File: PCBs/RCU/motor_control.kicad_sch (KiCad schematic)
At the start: 36 parts

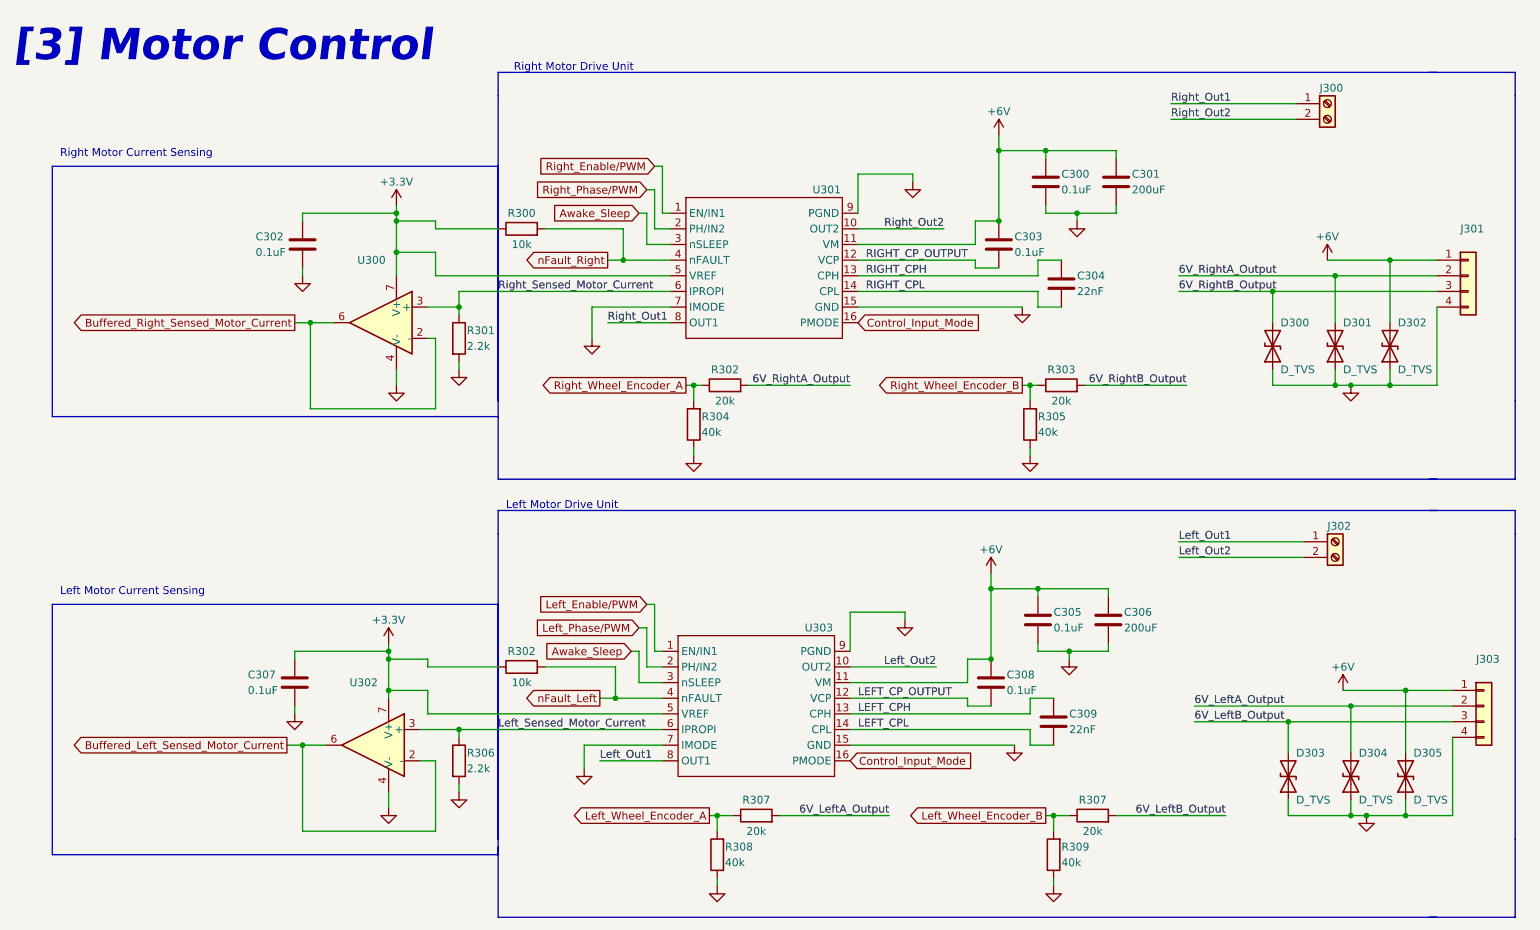
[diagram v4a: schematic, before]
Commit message: Add footprint to rest of IC's except ESP32
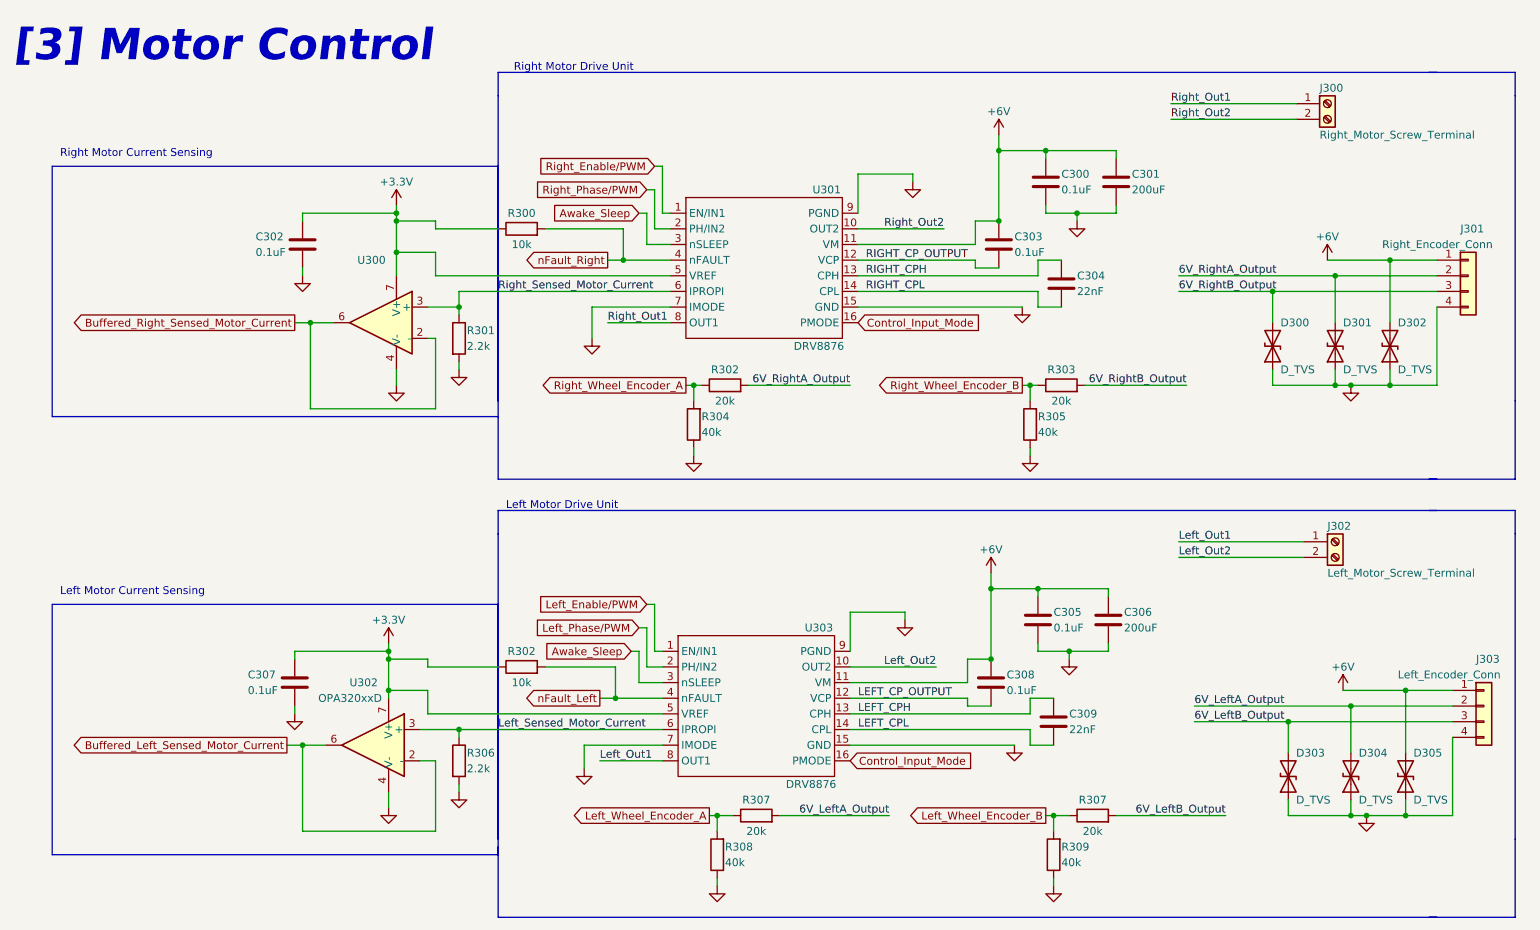
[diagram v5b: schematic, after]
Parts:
- J300: value (none) -> Right_Motor_Screw_Terminal; footprint (none) -> TerminalBlock:TerminalBlock_bornier-2_P5.08mm
- J301: value (none) -> Right_Encoder_Conn; footprint (none) -> Connector_PinHeader_2.54mm:PinHeader_1x04_P2.54mm_Vertical
- J302: value (none) -> Left_Motor_Screw_Terminal; footprint (none) -> TerminalBlock:TerminalBlock_bornier-2_P5.08mm
- J303: value (none) -> Left_Encoder_Conn; footprint (none) -> Connector_PinHeader_2.54mm:PinHeader_1x04_P2.54mm_Vertical
- U301, U303: value (none) -> DRV8876; footprint (none) -> Package_SO:HTSSOP-16-1EP_4.4x5mm_P0.65mm_EP3.4x5mm_Mask2.46x2.31mm_ThermalVias
- U302: value (none) -> OPA320xxD; footprint (none) -> Package_TO_SOT_SMD:SOT-23-5
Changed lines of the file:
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@@
     (in_bom yes) (on_board yes)
     (property "Reference" "U301" (id 0) (at 156.21 44.45 0))
-    (property "Value" "" (id 1) (at 154.94 69.85 0))
-    (property "Footprint" "" (id 2) (at 146.05 55.88 0)
+    (property "Value" "DRV8876" (id 1) (at 154.94 69.85 0))
+    (property "Footprint" "Package_SO:HTSSOP-16-1EP_4.4x5mm_P0.65mm_EP3.4x5mm_Mask2.46x2.31mm_ThermalVias" (id 2) (at 146.05 55.88 0)
       (effects (font (size 1.27 1.27)) hide)
     )
@@
       (effects (font (size 1.27 1.27)) (justify left))
     )
-    (property "Value" "" (id 1) (at 237.49 106.68 0)
-      (effects (font (size 1.27 1.27)) (justify left))
-    )
-    (property "Footprint" "" (id 2) (at 238.76 101.6 0)
+    (property "Value" "Left_Motor_Screw_Terminal" (id 1) (at 237.49 106.68 0)
+      (effects (font (size 1.27 1.27)) (justify left))
+    )
+    (property "Footprint" "TerminalBlock:TerminalBlock_bornier-2_P5.08mm" (id 2) (at 238.76 101.6 0)
       (effects (font (size 1.27 1.27)) hide)
     )
@@
       (effects (font (size 1.27 1.27)) (justify left))
     )
-    (property "Value" "" (id 1) (at 236.22 35.56 0)
-      (effects (font (size 1.27 1.27)) (justify left))
-    )
-    (property "Footprint" "" (id 2) (at 237.49 30.48 0)
+    (property "Value" "Right_Motor_Screw_Terminal" (id 1) (at 236.22 35.56 0)
+      (effects (font (size 1.27 1.27)) (justify left))
+    )
+    (property "Footprint" "TerminalBlock:TerminalBlock_bornier-2_P5.08mm" (id 2) (at 237.49 30.48 0)
       (effects (font (size 1.27 1.27)) hide)
     )
@@
       (effects (font (size 1.27 1.27)) (justify left))
     )
-    (property "Value" "" (id 1) (at 248.92 123.19 0)
-      (effects (font (size 1.27 1.27)) (justify left))
-    )
-    (property "Footprint" "" (id 2) (at 262.89 128.27 0)
+    (property "Value" "Left_Encoder_Conn" (id 1) (at 248.92 123.19 0)
+      (effects (font (size 1.27 1.27)) (justify left))
+    )
+    (property "Footprint" "Connector_PinHeader_2.54mm:PinHeader_1x04_P2.54mm_Vertical" (id 2) (at 262.89 128.27 0)
       (effects (font (size 1.27 1.27)) hide)
     )
@@
       (effects (font (size 1.27 1.27)) (justify left))
     )
-    (property "Value" "" (id 1) (at 246.38 53.34 0)
-      (effects (font (size 1.27 1.27)) (justify left))
-    )
-    (property "Footprint" "" (id 2) (at 260.35 58.42 0)
+    (property "Value" "Right_Encoder_Conn" (id 1) (at 246.38 53.34 0)
+      (effects (font (size 1.27 1.27)) (justify left))
+    )
+    (property "Footprint" "Connector_PinHeader_2.54mm:PinHeader_1x04_P2.54mm_Vertical" (id 2) (at 260.35 58.42 0)
       (effects (font (size 1.27 1.27)) hide)
     )
@@
     (in_bom yes) (on_board yes)
     (property "Reference" "U303" (id 0) (at 154.94 115.57 0))
-    (property "Value" "" (id 1) (at 153.67 140.97 0))
-    (property "Footprint" "" (id 2) (at 144.78 127 0)
+    (property "Value" "DRV8876" (id 1) (at 153.67 140.97 0))
+    (property "Footprint" "Package_SO:HTSSOP-16-1EP_4.4x5mm_P0.65mm_EP3.4x5mm_Mask2.46x2.31mm_ThermalVias" (id 2) (at 144.78 127 0)
       (effects (font (size 1.27 1.27)) hide)
     )
@@
       (effects (font (size 1.27 1.27)) (justify right))
     )
-    (property "Value" "" (id 1) (at 73.66 127 0)
-      (effects (font (size 1.27 1.27)) (justify right))
-    )
-    (property "Footprint" "" (id 2) (at 85.09 139.7 0)
+    (property "Value" "OPA320xxD" (id 1) (at 73.66 127 0)
+      (effects (font (size 1.27 1.27)) (justify right))
+    )
+    (property "Footprint" "Package_TO_SOT_SMD:SOT-23-5" (id 2) (at 85.09 139.7 0)
       (effects (font (size 1.27 1.27)) (justify left) hide)
     )

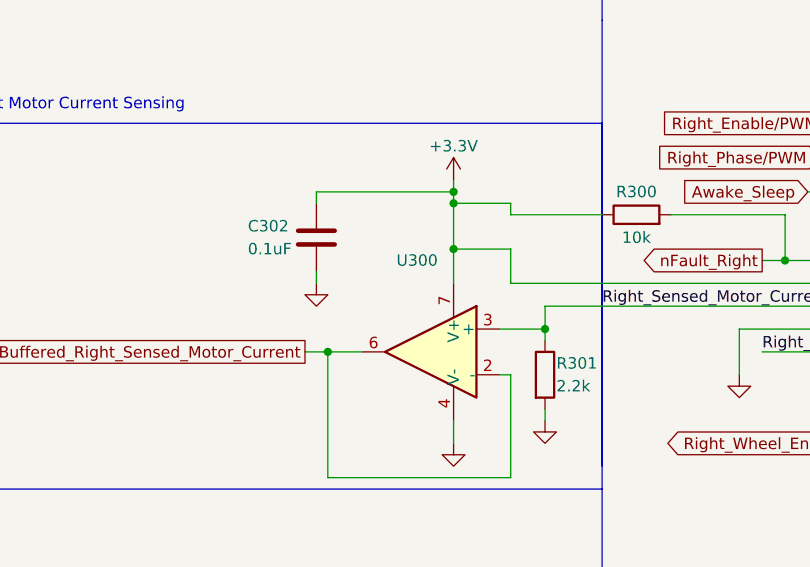
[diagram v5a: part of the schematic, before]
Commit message: Add footprint to power module diodes, and replaced 1N4148W with 2 SM5817's
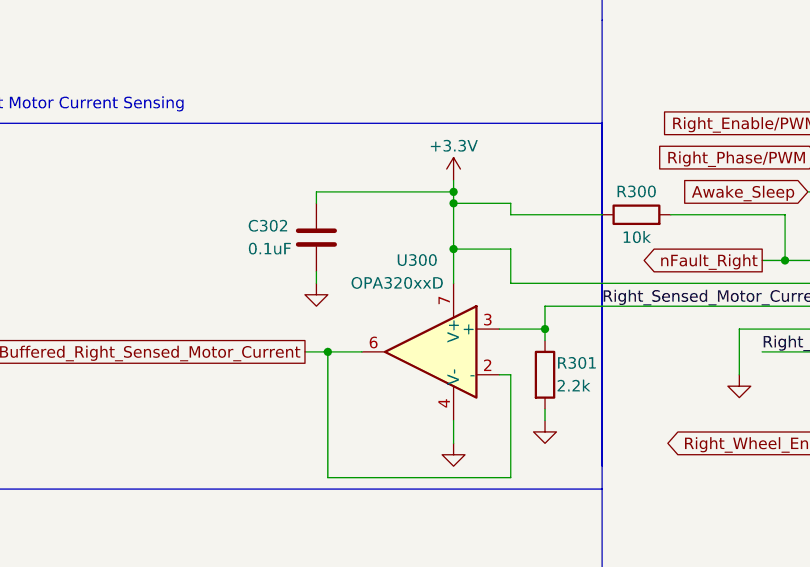
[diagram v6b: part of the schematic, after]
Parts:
- U300: value (none) -> OPA320xxD; footprint (none) -> Package_TO_SOT_SMD:SOT-23-5
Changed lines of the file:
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@@
       (effects (font (size 1.27 1.27)) (justify right))
     )
-    (property "Value" "" (id 1) (at 74.93 58.42 0)
+    (property "Value" "OPA320xxD" (id 1) (at 74.93 58.42 0)
       (effects (font (size 1.27 1.27)) (justify right))
     )
-    (property "Footprint" "" (id 2) (at 86.36 71.12 0)
+    (property "Footprint" "Package_TO_SOT_SMD:SOT-23-5" (id 2) (at 86.36 71.12 0)
       (effects (font (size 1.27 1.27)) (justify left) hide)
     )

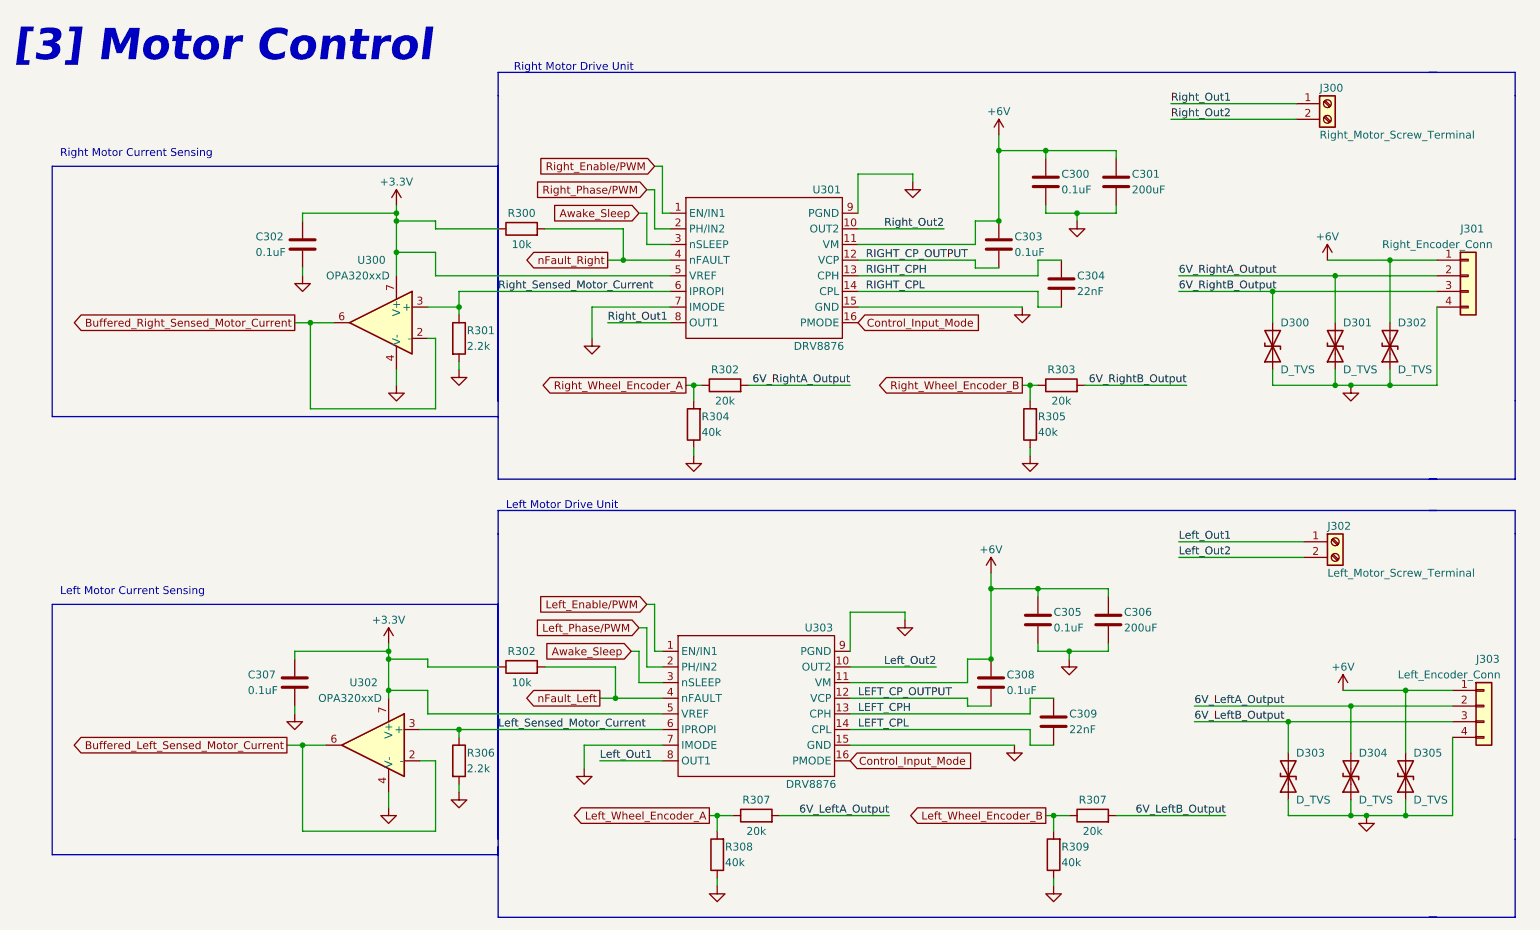
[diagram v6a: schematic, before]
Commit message: Add footrpints to TVS diodes in [3]
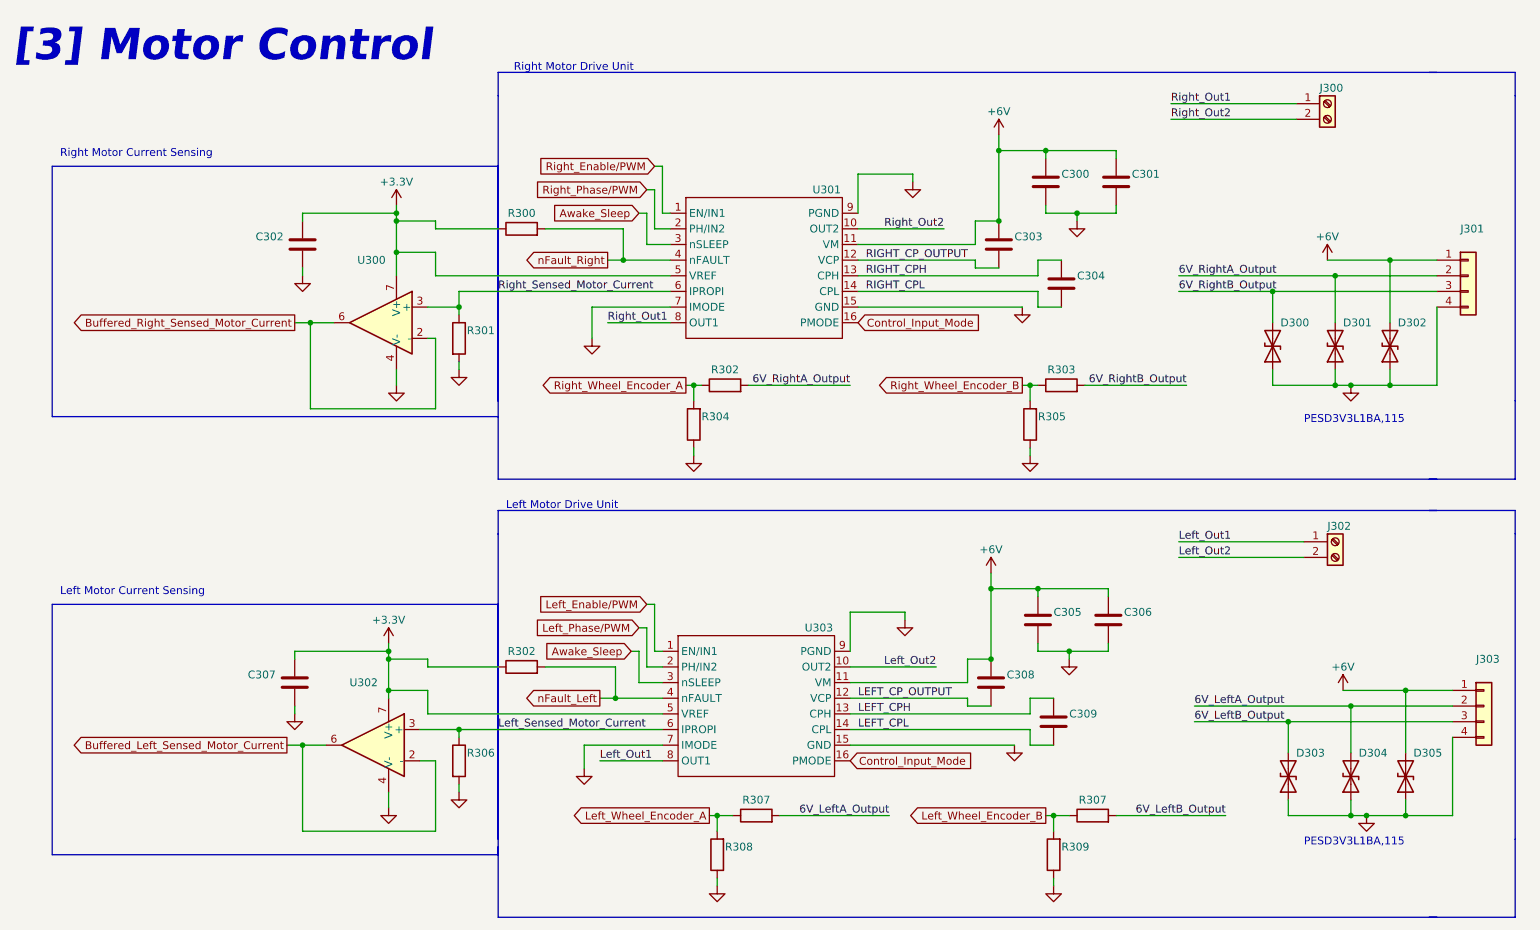
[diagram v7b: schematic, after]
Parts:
- C300, C302, C303, C305, C307, C308: value 0.1uF -> (none)
- C301, C306: value 200uF -> (none)
- C304, C309: value 22nF -> (none)
- D300, D301, D302, D303, D304, D305: value D_TVS -> (none)
- J300: value Right_Motor_Screw_Terminal -> (none); footprint TerminalBlock:TerminalBlock_bornier-2_P5.08mm -> (none)
- J301: value Right_Encoder_Conn -> (none); footprint Connector_PinHeader_2.54mm:PinHeader_1x04_P2.54mm_Vertical -> (none)
- J302: value Left_Motor_Screw_Terminal -> (none); footprint TerminalBlock:TerminalBlock_bornier-2_P5.08mm -> (none)
- J303: value Left_Encoder_Conn -> (none); footprint Connector_PinHeader_2.54mm:PinHeader_1x04_P2.54mm_Vertical -> (none)
- R300, R302: value 10k -> (none)
- R301, R306: value 2.2k -> (none)
- R302, R303, R307: value 20k -> (none)
- R304, R305, R308, R309: value 40k -> (none)
- U300, U302: value OPA320xxD -> (none); footprint Package_TO_SOT_SMD:SOT-23-5 -> (none)
- U301, U303: value DRV8876 -> (none); footprint Package_SO:HTSSOP-16-1EP_4.4x5mm_P0.65mm_EP3.4x5mm_Mask2.46x2.31mm_ThermalVias -> (none)
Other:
- note added: "PESD3V3L1BA,115"

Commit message: Passed ERC
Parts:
- C300, C302, C303, C305, C307, C308: value (none) -> 0.1uF; footprint (none) -> Capacitor_SMD:C_0603_1608Metric
- C301, C306: value (none) -> 220uF; footprint (none) -> Capacitor_THT:CP_Radial_D5.0mm_P2.50mm
- C304, C309: value (none) -> 22nF; footprint (none) -> Capacitor_SMD:C_0603_1608Metric
- D300, D301, D302, D303, D304, D305: value (none) -> PESD3V3L1BA,115; footprint (none) -> Diode_SMD:D_SOD-323
- J300: value (none) -> Right_Motor_Screw_Terminal; footprint (none) -> TerminalBlock:TerminalBlock_bornier-2_P5.08mm
- J301: value (none) -> Right_Encoder_Conn; footprint (none) -> Connector_PinHeader_2.54mm:PinHeader_1x04_P2.54mm_Vertical
- J302: value (none) -> Left_Motor_Screw_Terminal; footprint (none) -> TerminalBlock:TerminalBlock_bornier-2_P5.08mm
- J303: value (none) -> Left_Encoder_Conn; footprint (none) -> Connector_PinHeader_2.54mm:PinHeader_1x04_P2.54mm_Vertical
- R300: value (none) -> 10k; footprint (none) -> Resistor_SMD:R_0603_1608Metric
- R301: value (none) -> 2.2k; footprint (none) -> Resistor_SMD:R_0603_1608Metric
- R302, R303: value (none) -> 20k; footprint (none) -> Resistor_SMD:R_0603_1608Metric
- R304, R305: value (none) -> 40k; footprint (none) -> Resistor_SMD:R_0603_1608Metric
- R306: renamed from R302; value (none) -> 10k; footprint (none) -> Resistor_SMD:R_0603_1608Metric
- R307: renamed from R306; value (none) -> 2.2k; footprint (none) -> Resistor_SMD:R_0603_1608Metric
- R309: renamed from R307; value (none) -> 20k; footprint (none) -> Resistor_SMD:R_0603_1608Metric
- R310: renamed from R308; value (none) -> 40k; footprint (none) -> Resistor_SMD:R_0603_1608Metric
- R311: renamed from R309; value (none) -> 40k; footprint (none) -> Resistor_SMD:R_0603_1608Metric
- U300, U302: value (none) -> OPA320xxD; footprint (none) -> Package_TO_SOT_SMD:SOT-23-5
- U301, U303: value (none) -> DRV8876; footprint (none) -> Package_SO:HTSSOP-16-1EP_4.4x5mm_P0.65mm_EP3.4x5mm_Mask2.46x2.31mm_ThermalVias
- renumbered R307 to R308
